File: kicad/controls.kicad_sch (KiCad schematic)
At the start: 4 parts, among them P1 Potentiometer_9mm_Vertical_Li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, P2 Potentiometer_9mm_Vertical_Li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, SW1 SW_Push_LED, SW2 SW_Push_LED

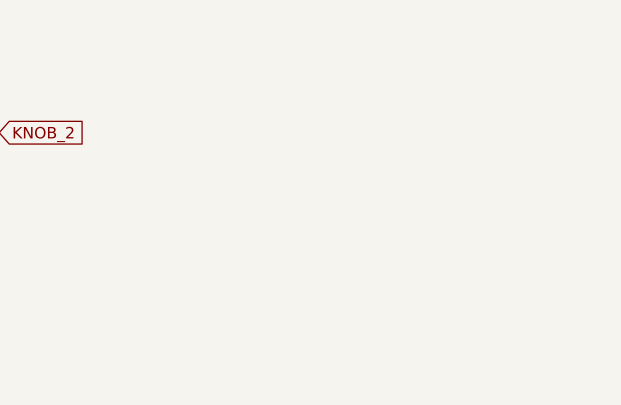
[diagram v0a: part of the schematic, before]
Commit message: input changes
use single channel ADCs for analog inputs and knob 1 which use i2c instead of SPI to free up one pin for input 1 to be used as a digital input as well
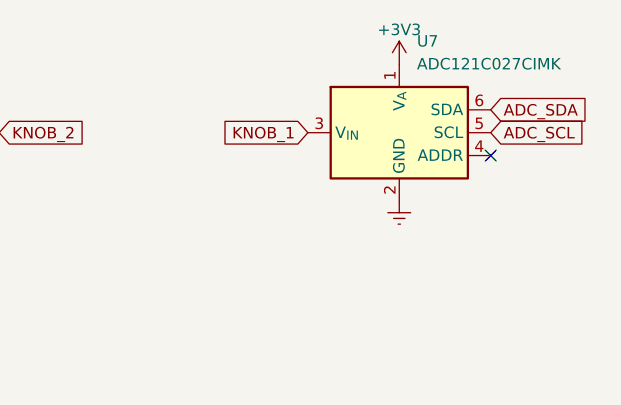
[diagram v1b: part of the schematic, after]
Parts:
- added U7: ADC121C027CIMK, Package_TO_SOT_SMD:TSOT-23-6, symbol Analog_ADC:ADC101C021CIMK
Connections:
- net +3V3: now also U7.1 (V_{A})
- net Earth: now also U7.2 (GND)
- net KNOB_1: now also U7.3 (V_{IN})
- new net ADC_SCL: U7.5 (SCL)
- new net ADC_SDA: U7.6 (SDA)
- no-connect marks 8 -> 9
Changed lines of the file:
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@@
   (no_connect (at 46.99 71.12))
   (no_connect (at 46.99 105.41))
+  (no_connect (at 123.19 39.37))
   (no_connect (at 59.69 71.12))
   (no_connect (at 46.99 76.2))
@@
     (stroke (width 0) (type default))
   )
+  (global_label "ADC_SCL" (shape input) (at 123.19 36.83 0) (fields_autoplaced)
+    (effects (font (size 1.27 1.27)) (justify left))
+    (property "Intersheetrefs" "${INTERSHEET_REFS}" (at 134.1996 36.83 0)
+      (effects (font (size 1.27 1.27)) (justify left) hide)
+    )
+  )
   (global_label "KNOB_2" (shape input) (at 68.58 36.83 0) (fields_autoplaced)
     (effects (font (size 1.27 1.27)) (justify left))
     (property "Intersheetrefs" "${INTERSHEET_REFS}" (at 78.8639 36.83 0)
+      (effects (font (size 1.27 1.27)) (justify left) hide)
+    )
+  )
+  (global_label "ADC_SDA" (shape input) (at 123.19 34.29 0) (fields_autoplaced)
+    (effects (font (size 1.27 1.27)) (justify left))
+    (property "Intersheetrefs" "${INTERSHEET_REFS}" (at 134.2601 34.29 0)
       (effects (font (size 1.27 1.27)) (justify left) hide)
     )
@@
     (effects (font (size 1.27 1.27)) (justify right))
     (property "Intersheetrefs" "${INTERSHEET_REFS}" (at 28.3604 81.28 0)
+      (effects (font (size 1.27 1.27)) (justify right) hide)
+    )
+  )
+  (global_label "KNOB_1" (shape input) (at 102.87 36.83 180) (fields_autoplaced)
+    (effects (font (size 1.27 1.27)) (justify right))
+    (property "Intersheetrefs" "${INTERSHEET_REFS}" (at 92.5861 36.83 0)
       (effects (font (size 1.27 1.27)) (justify right) hide)
     )
@@
         )
       )
+    )
+  )
+  (symbol (lib_id "Analog_ADC:ADC101C021CIMK") (at 113.03 36.83 0) (unit 1)
+    (in_bom yes) (on_board yes) (dnp no) (fields_autoplaced)
+    (property "Reference" "U7" (at 114.9859 26.67 0)
+      (effects (font (size 1.27 1.27)) (justify left))
+    )
+    (property "Value" "ADC121C027CIMK" (at 114.9859 29.21 0)
+      (effects (font (size 1.27 1.27)) (justify left))
+    )
+    (property "Footprint" "Package_TO_SOT_SMD:TSOT-23-6" (at 113.03 36.83 0)
+      (effects (font (size 1.27 1.27)) hide)
+    )
+    (property "Datasheet" "https://www.ti.com/lit/ds/symlink/adc101c021.pdf" (at 113.03 36.83 0)
+      (effects (font (size 1.27 1.27)) hide)
+    )
+    (pin "1")
+    (pin "2")
+    (pin "3")
+    (pin "4")
+    (pin "5")
+    (pin "6")
+    (instances
+      (project "EuroPi LC"
+        (path "/1702e620-a749-4340-9e49-cfdb2636cab7"
+          (reference "U7") (unit 1)
+        )
+        (path "/1702e620-a749-4340-9e49-cfdb2636cab7/8b492937-b70b-4e04-a312-87c396a83887"
+          (reference "U5") (unit 1)
+        )
+        (path "/1702e620-a749-4340-9e49-cfdb2636cab7/8a49e3e8-3b89-4e8d-909c-39ca22ceb2c2"
+          (reference "U7") (unit 1)
+        )
+      )
+    )
+  )
+  (symbol (lib_id "power:Earth") (at 113.03 44.45 0) (unit 1)
+    (in_bom yes) (on_board yes) (dnp no) (fields_autoplaced)
+    (property "Reference" "#PWR042" (at 113.03 50.8 0)
+      (effects (font (size 1.27 1.27)) hide)
+    )
+    (property "Value" "Earth" (at 113.03 48.26 0)
+      (effects (font (size 1.27 1.27)) hide)
+    )
+    (property "Footprint" "" (at 113.03 44.45 0)
+      (effects (font (size 1.27 1.27)) hide)
+    )
+    (property "Datasheet" "~" (at 113.03 44.45 0)
+      (effects (font (size 1.27 1.27)) hide)
+    )
+    (pin "1")
+    (instances
+      (project "EuroPi LC"
+        (path "/1702e620-a749-4340-9e49-cfdb2636cab7"
+          (reference "#PWR042") (unit 1)
+        )
+        (path "/1702e620-a749-4340-9e49-cfdb2636cab7/8b492937-b70b-4e04-a312-87c396a83887"
+          (reference "#PWR032") (unit 1)
+        )
+        (path "/1702e620-a749-4340-9e49-cfdb2636cab7/8a49e3e8-3b89-4e8d-909c-39ca22ceb2c2"
+          (reference "#PWR042") (unit 1)
+        )
+      )
+    )
+  )
+  (symbol (lib_id "power:+3V3") (at 113.03 29.21 0) (unit 1)
+    (in_bom yes) (on_board yes) (dnp no) (fields_autoplaced)
+    (property "Reference" "#PWR031" (at 113.03 33.02 0)
+      (effects (font (size 1.27 1.27)) hide)
+    )
+    (property "Value" "+3V3" (at 113.03 25.4 0)
+      (effects (font (size 1.27 1.27)))
+    )
+    (property "Footprint" "" (at 113.03 29.21 0)
+      (effects (font (size 1.27 1.27)) hide)
+    )
+    (property "Datasheet" "" (at 113.03 29.21 0)
+      (effects (font (size 1.27 1.27)) hide)
+    )
+    (pin "1")
+    (instances
+      (project "EuroPi LC"
+        (path "/1702e620-a749-4340-9e49-cfdb2636cab7"
+          (reference "#PWR031") (unit 1)
+        )
+        (path "/1702e620-a749-4340-9e49-cfdb2636cab7/8b492937-b70b-4e04-a312-87c396a83887"
+          (reference "#PWR041") (unit 1)
+        )
+        (path "/1702e620-a749-4340-9e49-cfdb2636cab7/8a49e3e8-3b89-4e8d-909c-39ca22ceb2c2"
+          (reference "#PWR031") (unit 1)
+        )
+      )

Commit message: reroute pcb
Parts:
- P1, P2: footprint Eurorack:Potentiometer 9mm Vertical Linear Centred -> allen-synthesis:potentiometer-9mm
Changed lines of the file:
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@@
       (effects (font (size 1.27 1.27)) (justify right) hide)
     )
-    (property "Footprint" "Eurorack:Potentiometer 9mm Vertical Linear Centred" (at 27.94 34.29 0)
+    (property "Footprint" "allen-synthesis:potentiometer-9mm" (at 27.94 34.29 0)
       (effects (font (size 1.27 1.27)) hide)
     )
@@
       (effects (font (size 1.27 1.27)) (justify right) hide)
     )
-    (property "Footprint" "Eurorack:Potentiometer 9mm Vertical Linear Centred" (at 59.69 34.29 0)
+    (property "Footprint" "allen-synthesis:potentiometer-9mm" (at 59.69 34.29 0)
       (effects (font (size 1.27 1.27)) hide)
     )

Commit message: add schematic notes
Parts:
- added C9: 100n, Capacitor_SMD:C_0402_1005Metric, symbol Device:C
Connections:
- net +3V3: now also C9.1
- net Earth: now also C9.2
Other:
- note added: "The buttons have built in LEDs, however the lack of pins on the XIAO RP2040 means they aren't used"
- note added: "The potentiometers used for the knobs simply divides the 3.3V rail to ground"
- moved on the sheet: P2, SW1, SW2, U7
